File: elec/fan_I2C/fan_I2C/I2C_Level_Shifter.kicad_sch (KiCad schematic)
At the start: 17 parts, among them J201 S04B-XASK-1(LF)(SN), J202 0.100_2Pin, Q201 BSS138, Q202 BSS138

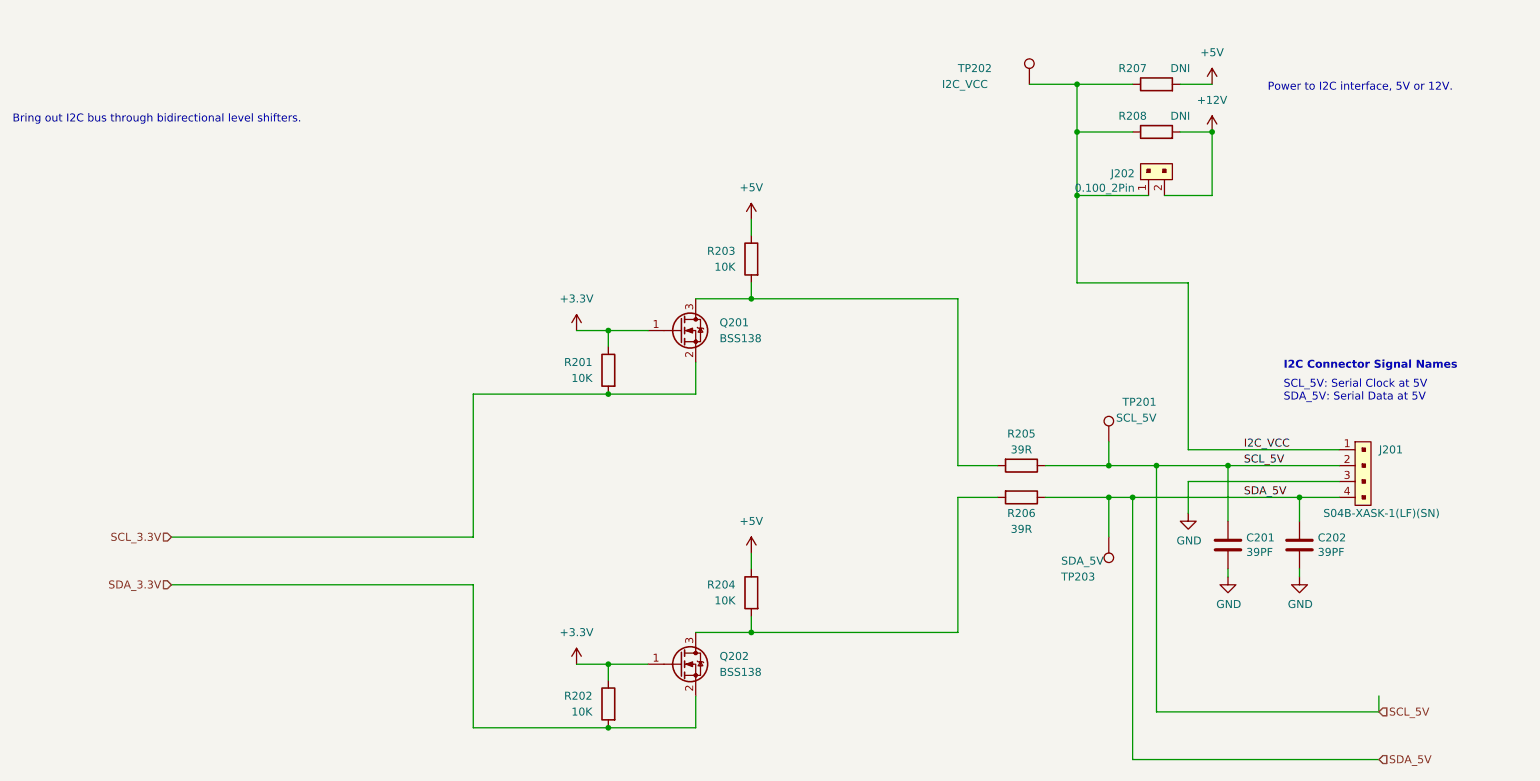
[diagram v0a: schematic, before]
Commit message: Making power local to the sheets.
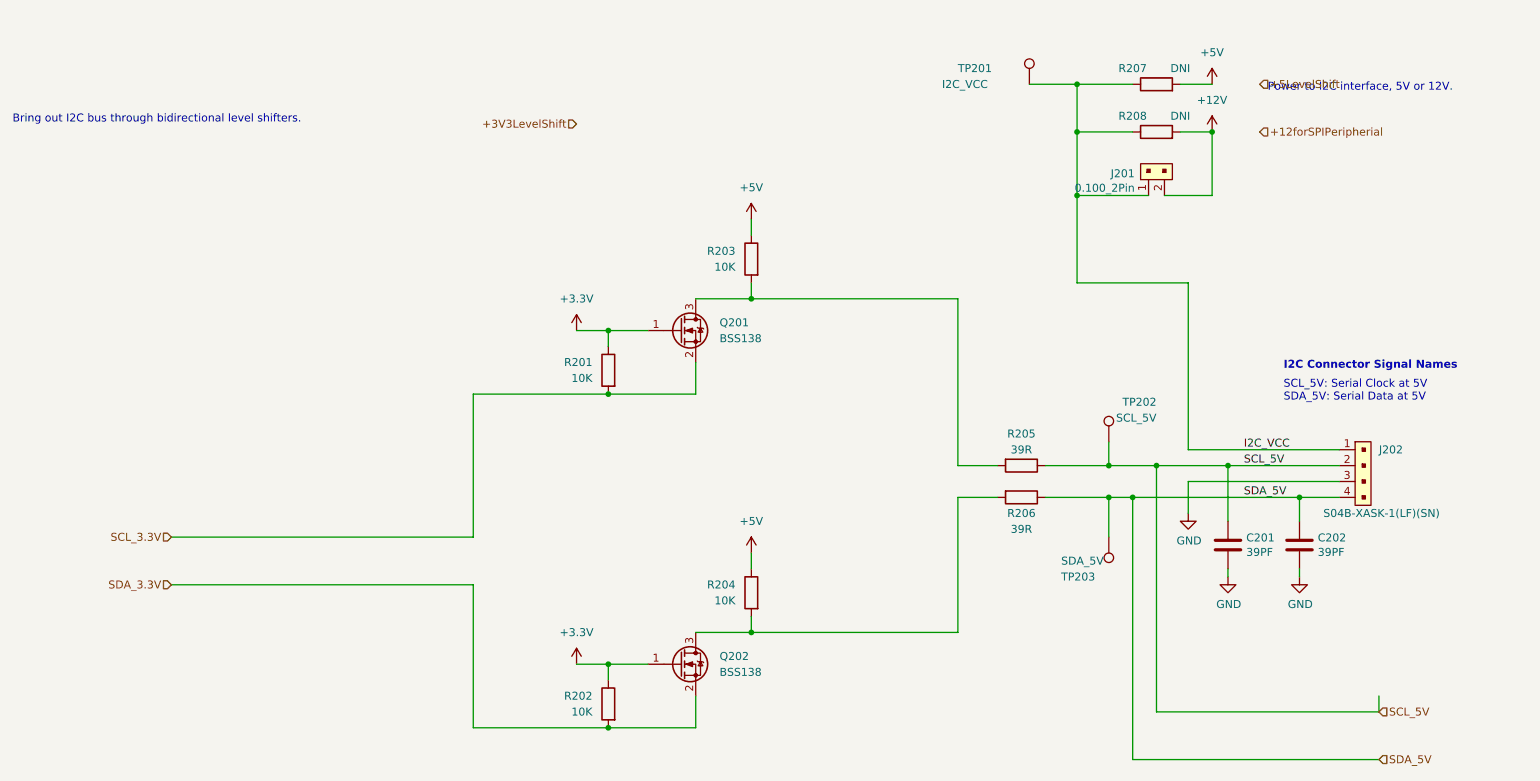
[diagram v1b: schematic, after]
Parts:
- renumbered J202 to J201, J201 to J202, TP202 to TP201, TP201 to TP202
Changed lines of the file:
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@@
+    (effects (font (size 1.27 1.27)) (justify right))
+  )
+  (hierarchical_label "+3V3LevelShift" (shape input) (at 119.38 31.75 180)
     (effects (font (size 1.27 1.27)) (justify right))
   )
@@
   (hierarchical_label "SCL_3.3V" (shape input) (at 54.61 97.79 180)
     (effects (font (size 1.27 1.27)) (justify right))
+  )
+  (hierarchical_label "+5LevelShift" (shape input) (at 228.6 25.4 0)
+    (effects (font (size 1.27 1.27)) (justify left))
+  )
+  (hierarchical_label "+12forSPIPeripherial" (shape input) (at 228.6 33.02 0)
+    (effects (font (size 1.27 1.27)) (justify left))
   )
   (symbol (lib_id "Device:R") (at 190.5 86.36 270) (unit 1)
@@
   (symbol (lib_id "Connector:TestPoint") (at 191.77 25.4 0) (unit 1)
     (in_bom yes) (on_board yes)
-    (property "Reference" "TP202" (id 0) (at 180.34 22.86 0)
+    (property "Reference" "TP201" (id 0) (at 180.34 22.86 0)
       (effects (font (size 1.27 1.27)) (justify left))
     )
@@
   (symbol (lib_id "GPAD_SCH_LIB:22-23-2021") (at 210.82 40.64 0) (mirror x) (unit 1)
     (in_bom yes) (on_board yes)
-    (property "Reference" "J202" (id 0) (at 208.6102 39.6748 0)
+    (property "Reference" "J201" (id 0) (at 208.6102 39.6748 0)
       (effects (font (size 1.27 1.27)) (justify right))
     )
@@
   (symbol (lib_id "Connector:TestPoint") (at 204.47 82.55 0) (mirror y) (unit 1)
     (in_bom yes) (on_board yes)
-    (property "Reference" "TP201" (id 0) (at 212.09 76.2 0)
+    (property "Reference" "TP202" (id 0) (at 212.09 76.2 0)
       (effects (font (size 1.27 1.27)) (justify left))
     )
@@
   (symbol (lib_id "GPAD_SCH_LIB:S04B-XASK-1(LF)(SN)") (at 243.84 83.82 90) (mirror x) (unit 1)
     (in_bom yes) (on_board yes)
-    (property "Reference" "J201" (id 0) (at 247.65 83.82 90)
+    (property "Reference" "J202" (id 0) (at 247.65 83.82 90)
       (effects (font (size 1.27 1.27)) (justify right))
     )

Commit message: Add Connectors RJ12 and JST.
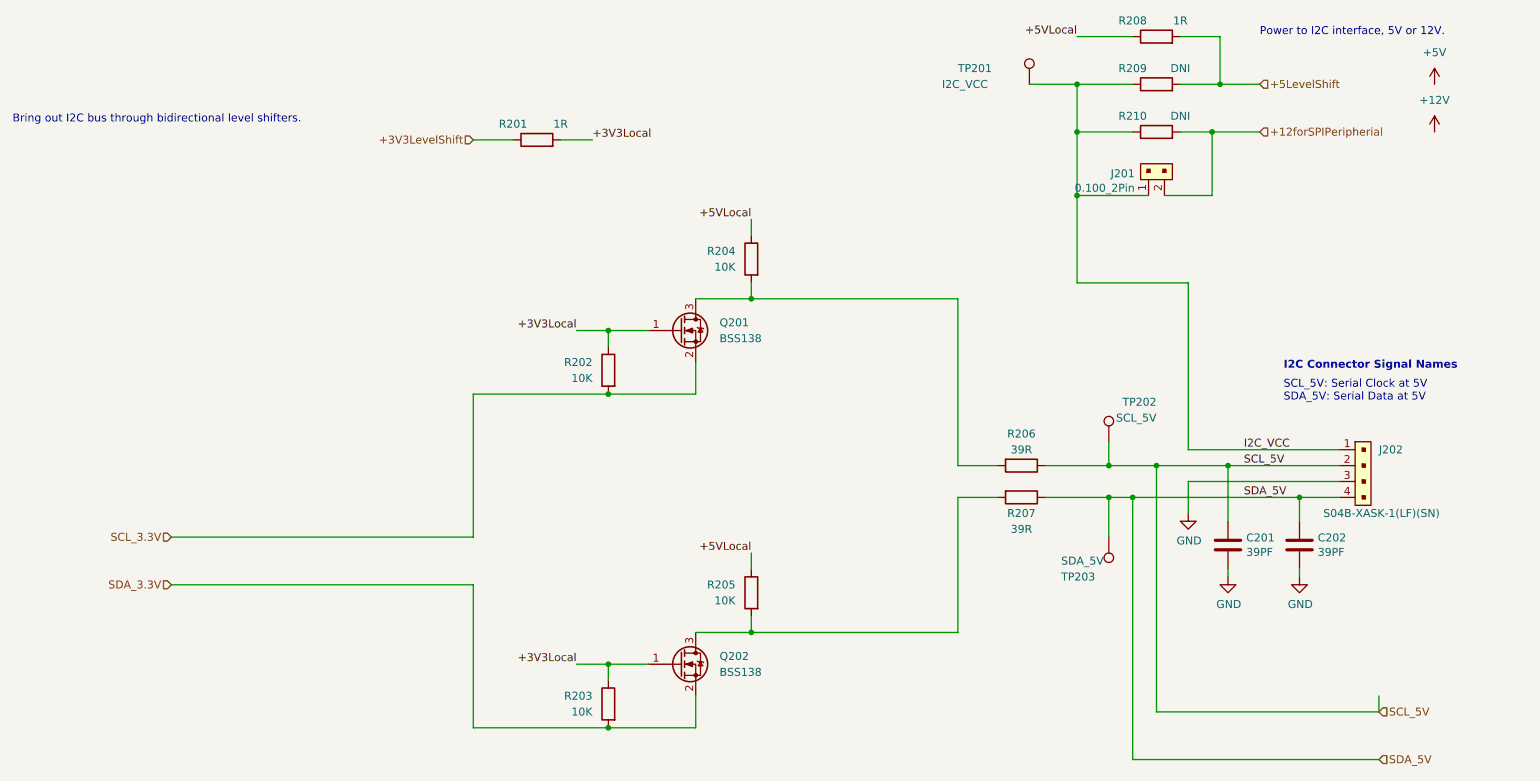
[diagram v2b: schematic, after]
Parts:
- added R201, R208: 1R, Resistor_SMD:R_0603_1608Metric_Pad0.98x0.95mm_HandSolder, symbol Device:R
- renumbered R201 to R202, R202 to R203, R203 to R204, R204 to R205, R205 to R206, R206 to R207, R207 to R209, R208 to R210
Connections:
- net +12V: no longer J201.2, R210.2
- net +12forSPIPeripherial: now also J201.2, R210.2
- net +3V3LevelShift: now also R201.1
- net +5LevelShift: now also R209.2, R208.2
- net +5V: no longer R204.1, R205.1, R209.2
- net +3.3V renamed +3V3Local
- net +3V3Local: now also R201.2
- new net +5VLocal: R204.1, R205.1, R208.1

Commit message: Add Connectors like Roberts Fritzing.
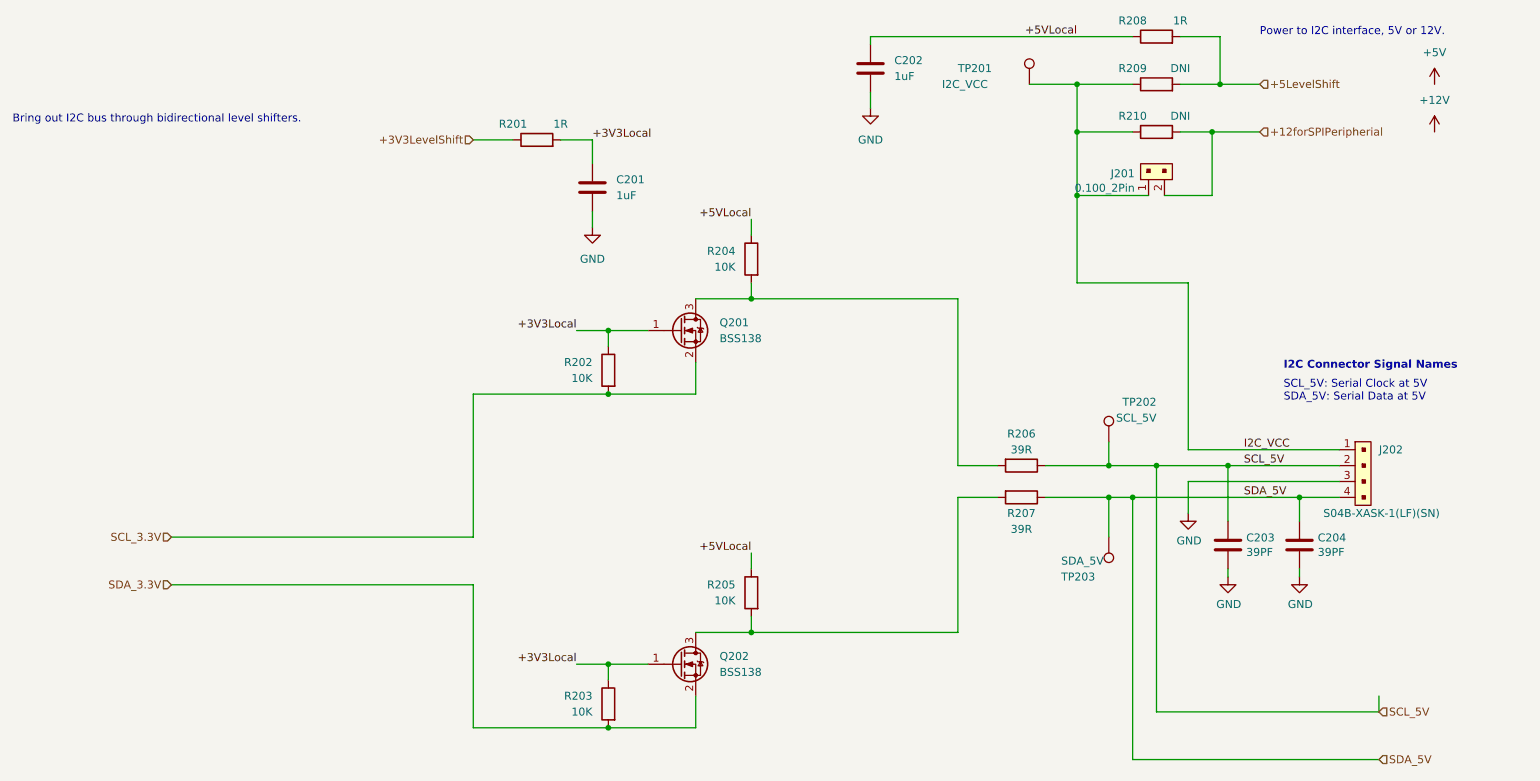
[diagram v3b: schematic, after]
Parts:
- added C201, C202: 1uF, Capacitor_SMD:C_0603_1608Metric_Pad1.08x0.95mm_HandSolder, symbol Device:C
- renumbered C201 to C203, C202 to C204
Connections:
- net +3V3Local: now also C201.1
- net +5VLocal: now also C202.1
- net GND: now also C201.2, C202.2
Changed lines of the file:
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@@
     (stroke (width 0) (type default) (color 0 0 0 0))
   )
-  (wire (pts (xy 199.39 17.78) (xy 208.28 17.78))
+  (wire (pts (xy 166.37 17.78) (xy 208.28 17.78))
     (stroke (width 0) (type default) (color 0 0 0 0))
   )
@@
     (stroke (width 0) (type default) (color 0 0 0 0))
   )
+  (wire (pts (xy 121.92 45.72) (xy 121.92 48.26))
+    (stroke (width 0) (type default) (color 0 0 0 0))
+  )
   (wire (pts (xy 247.65 123.19) (xy 247.65 125.73))
     (stroke (width 0) (type default) (color 0 0 0 0))
@@
     (stroke (width 0) (type default) (color 0 0 0 0))
   )
+  (wire (pts (xy 166.37 17.78) (xy 166.37 19.05))
+    (stroke (width 0) (type default) (color 0 0 0 0))
+  )
   (wire (pts (xy 116.84 34.29) (xy 121.92 34.29))
     (stroke (width 0) (type default) (color 0 0 0 0))
@@
   )
   (wire (pts (xy 180.34 91.44) (xy 180.34 113.03))
+    (stroke (width 0) (type default) (color 0 0 0 0))
+  )
+  (wire (pts (xy 121.92 34.29) (xy 121.92 38.1))
+    (stroke (width 0) (type default) (color 0 0 0 0))
+  )
+  (wire (pts (xy 166.37 26.67) (xy 166.37 29.21))
     (stroke (width 0) (type default) (color 0 0 0 0))
   )
@@
   (symbol (lib_id "power:+5V") (at 256.54 25.4 0) (unit 1)
     (in_bom yes) (on_board yes) (fields_autoplaced)
-    (property "Reference" "#PWR0204" (id 0) (at 256.54 29.21 0)
+    (property "Reference" "#PWR0206" (id 0) (at 256.54 29.21 0)
       (effects (font (size 1.27 1.27)) hide)
     )
@@
     (pin "2")
   )
+  (symbol (lib_id "Device:C") (at 166.37 22.86 0) (unit 1)
+    (in_bom yes) (on_board yes) (fields_autoplaced)
+    (property "Reference" "C202" (id 0) (at 170.18 21.5899 0)
+      (effects (font (size 1.27 1.27)) (justify left))
+    )
+    (property "Value" "1uF" (id 1) (at 170.18 24.1299 0)
+      (effects (font (size 1.27 1.27)) (justify left))
+    )
+    (property "Footprint" "Capacitor_SMD:C_0603_1608Metric_Pad1.08x0.95mm_HandSolder" (id 2) (at 167.3352 26.67 0)
+      (effects (font (size 1.27 1.27)) hide)
+    )
+    (property "Datasheet" "https://datasheet.lcsc.com/lcsc/1811082118_YAGEO-CC0603JRNPO9BN390_C107049.pdf" (id 3) (at 166.37 22.86 0)
+      (effects (font (size 1.27 1.27)) hide)
+    )
+    (property "AssemblyType" "SMT" (id 4) (at 166.37 22.86 0)
+      (effects (font (size 1.27 1.27)) hide)
+    )
+    (property "Distributor 1" "JLCPCB" (id 5) (at 166.37 22.86 0)
+      (effects (font (size 1.27 1.27)) hide)
+    )
+    (property "Distributor 1 PN" "" (id 6) (at 166.37 22.86 0)
+      (effects (font (size 1.27 1.27)) hide)
+    )
+    (property "Cost" "0.0025" (id 7) (at 166.37 22.86 0)
+      (effects (font (size 1.27 1.27)) hide)
+    )
+    (property "MPN" "" (id 8) (at 166.37 22.86 0)
+      (effects (font (size 1.27 1.27)) hide)
+    )
+    (property "Manufacturer" "YAGEO" (id 9) (at 166.37 22.86 0)
+      (effects (font (size 1.27 1.27)) hide)
+    )
+    (property "LongLead" "NO" (id 10) (at 166.37 22.86 0)
+      (effects (font (size 1.27 1.27)) hide)
+    )
+    (property "Description" "50V 1uF ±5% 0603 Multilayer Ceramic Ca" (id 11) (at 166.37 22.86 0)
+      (effects (font (size 1.27 1.27)) hide)
+    )
+    (pin "1")
+    (pin "2")
+  )
+  (symbol (lib_id "power:GND") (at 166.37 29.21 0) (unit 1)
+    (in_bom yes) (on_board yes) (fields_autoplaced)
+    (property "Reference" "#PWR0202" (id 0) (at 166.37 35.56 0)
+      (effects (font (size 1.27 1.27)) hide)
+    )
+    (property "Value" "GND" (id 1) (at 166.37 34.29 0))
+    (property "Footprint" "" (id 2) (at 166.37 29.21 0)
+      (effects (font (size 1.27 1.27)) hide)
+    )
+    (property "Datasheet" "" (id 3) (at 166.37 29.21 0)
+      (effects (font (size 1.27 1.27)) hide)
+    )
+    (pin "1")
+  )
   (symbol (lib_id "Connector:TestPoint") (at 204.47 97.79 0) (mirror x) (unit 1)
     (in_bom yes) (on_board yes)
@@
   (symbol (lib_id "power:GND") (at 217.17 93.98 0) (unit 1)
     (in_bom yes) (on_board yes)
-    (property "Reference" "#PWR0201" (id 0) (at 217.17 100.33 0)
+    (property "Reference" "#PWR0203" (id 0) (at 217.17 100.33 0)
       (effects (font (size 1.27 1.27)) hide)
     )
@@
   (symbol (lib_id "power:GND") (at 234.95 104.14 0) (unit 1)
     (in_bom yes) (on_board yes)
-    (property "Reference" "#PWR0203" (id 0) (at 234.95 110.49 0)
+    (property "Reference" "#PWR0205" (id 0) (at 234.95 110.49 0)
       (effects (font (size 1.27 1.27)) hide)
     )
@@
     )
     (property "Datasheet" "" (id 3) (at 234.95 104.14 0)
+      (effects (font (size 1.27 1.27)) hide)
+    )
+    (pin "1")
+  )
+  (symbol (lib_id "Device:C") (at 121.92 41.91 0) (unit 1)
+    (in_bom yes) (on_board yes) (fields_autoplaced)
+    (property "Reference" "C201" (id 0) (at 125.73 40.6399 0)
+      (effects (font (size 1.27 1.27)) (justify left))
+    )
+    (property "Value" "1uF" (id 1) (at 125.73 43.1799 0)
+      (effects (font (size 1.27 1.27)) (justify left))
+    )
+    (property "Footprint" "Capacitor_SMD:C_0603_1608Metric_Pad1.08x0.95mm_HandSolder" (id 2) (at 122.8852 45.72 0)
+      (effects (font (size 1.27 1.27)) hide)
+    )
+    (property "Datasheet" "https://datasheet.lcsc.com/lcsc/1811082118_YAGEO-CC0603JRNPO9BN390_C107049.pdf" (id 3) (at 121.92 41.91 0)
+      (effects (font (size 1.27 1.27)) hide)
+    )
+    (property "AssemblyType" "SMT" (id 4) (at 121.92 41.91 0)
+      (effects (font (size 1.27 1.27)) hide)
+    )
+    (property "Distributor 1" "JLCPCB" (id 5) (at 121.92 41.91 0)
+      (effects (font (size 1.27 1.27)) hide)
+    )
+    (property "Distributor 1 PN" "" (id 6) (at 121.92 41.91 0)
+      (effects (font (size 1.27 1.27)) hide)
+    )
+    (property "Cost" "0.0025" (id 7) (at 121.92 41.91 0)
+      (effects (font (size 1.27 1.27)) hide)
+    )
+    (property "MPN" "" (id 8) (at 121.92 41.91 0)
+      (effects (font (size 1.27 1.27)) hide)
+    )
+    (property "Manufacturer" "YAGEO" (id 9) (at 121.92 41.91 0)
+      (effects (font (size 1.27 1.27)) hide)
+    )
+    (property "LongLead" "NO" (id 10) (at 121.92 41.91 0)
+      (effects (font (size 1.27 1.27)) hide)
+    )
+    (property "Description" "50V 1uF ±5% 0603 Multilayer Ceramic Ca" (id 11) (at 121.92 41.91 0)
+      (effects (font (size 1.27 1.27)) hide)
+    )
+    (pin "1")
+    (pin "2")
+  )
+  (symbol (lib_id "power:GND") (at 121.92 48.26 0) (unit 1)
+    (in_bom yes) (on_board yes) (fields_autoplaced)
+    (property "Reference" "#PWR0201" (id 0) (at 121.92 54.61 0)
+      (effects (font (size 1.27 1.27)) hide)
+    )
+    (property "Value" "GND" (id 1) (at 121.92 53.34 0))
+    (property "Footprint" "" (id 2) (at 121.92 48.26 0)
+      (effects (font (size 1.27 1.27)) hide)
+    )
+    (property "Datasheet" "" (id 3) (at 121.92 48.26 0)
       (effects (font (size 1.27 1.27)) hide)
     )
@@
   (symbol (lib_id "power:GND") (at 223.52 104.14 0) (unit 1)
     (in_bom yes) (on_board yes)
-    (property "Reference" "#PWR0202" (id 0) (at 223.52 110.49 0)
+    (property "Reference" "#PWR0204" (id 0) (at 223.52 110.49 0)
       (effects (font (size 1.27 1.27)) hide)
     )
@@
   (symbol (lib_id "Device:C") (at 234.95 99.06 0) (unit 1)
     (in_bom yes) (on_board yes)
-    (property "Reference" "C202" (id 0) (at 237.871 97.8916 0)
+    (property "Reference" "C204" (id 0) (at 237.871 97.8916 0)
       (effects (font (size 1.27 1.27)) (justify left))
     )
@@
   (symbol (lib_id "Device:C") (at 223.52 99.06 0) (unit 1)
     (in_bom yes) (on_board yes)
-    (property "Reference" "C201" (id 0) (at 226.441 97.8916 0)
+    (property "Reference" "C203" (id 0) (at 226.441 97.8916 0)
       (effects (font (size 1.27 1.27)) (justify left))
     )
@@
   (symbol (lib_id "power:+12V") (at 256.54 33.02 0) (unit 1)
     (in_bom yes) (on_board yes) (fields_autoplaced)
-    (property "Reference" "#PWR0205" (id 0) (at 256.54 36.83 0)
-      (effects (font (size 1.27 1.27)) hide)
-    )
+    (property "Reference" "#PWR0207" (id 0) (at 256.54 36.83 0)
+      (effects (font (size 1.27 1.27)) hide)
+    )
